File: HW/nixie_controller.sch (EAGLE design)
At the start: 200 parts, among them IC1 INA138, IC10 LD1117S33TR, IC11 74HC595D, IC2 LM386M-1, IC3 7812TV, IC4 DG408DYTSSOP-16, IC5 OPA317DBV, IC6 OPA317DBV, IC7 OPA340U, IC8 OPA340U, IC9 NE555D, J1 POWER_JACKPTH_LOCK, Q10 DMP3099L-7, Q11 MMBT3906, Q2 CMPT5551, Q3 CMPT5551, Q4 CMPT5551, Q5 FMMT558QTA, Q6 CMPT5551, Q7 MMBT3906, Q8 CMPT5551, Q9 CMPT5551, T1 MMBT3904, T2 MMBT3904

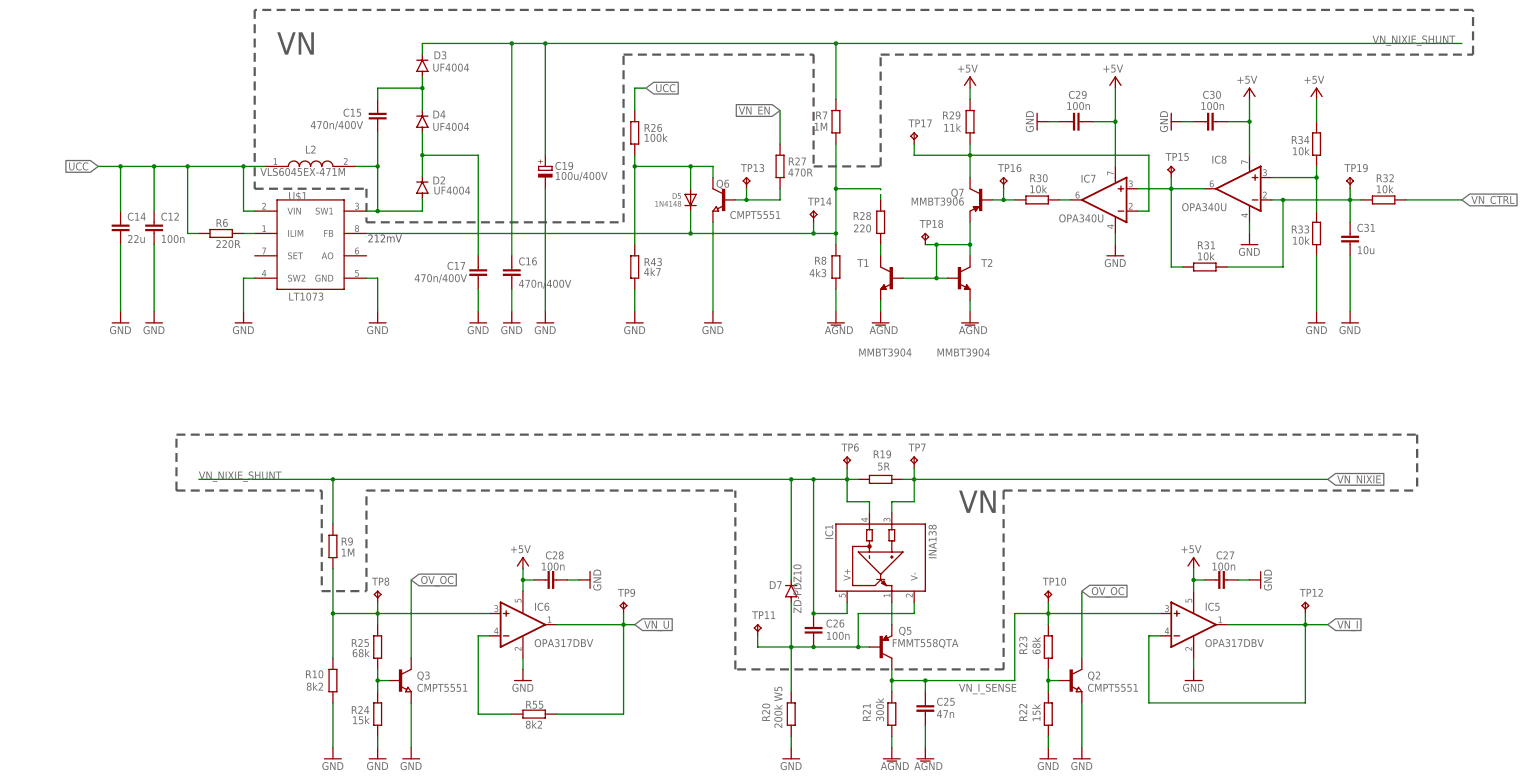
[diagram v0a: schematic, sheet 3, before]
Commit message: Update HW, SW - hlavne SW blizke HW, hodiny funkcni, bezi testovaci sekvence, na zmacknuti tlacitka se zobrazi
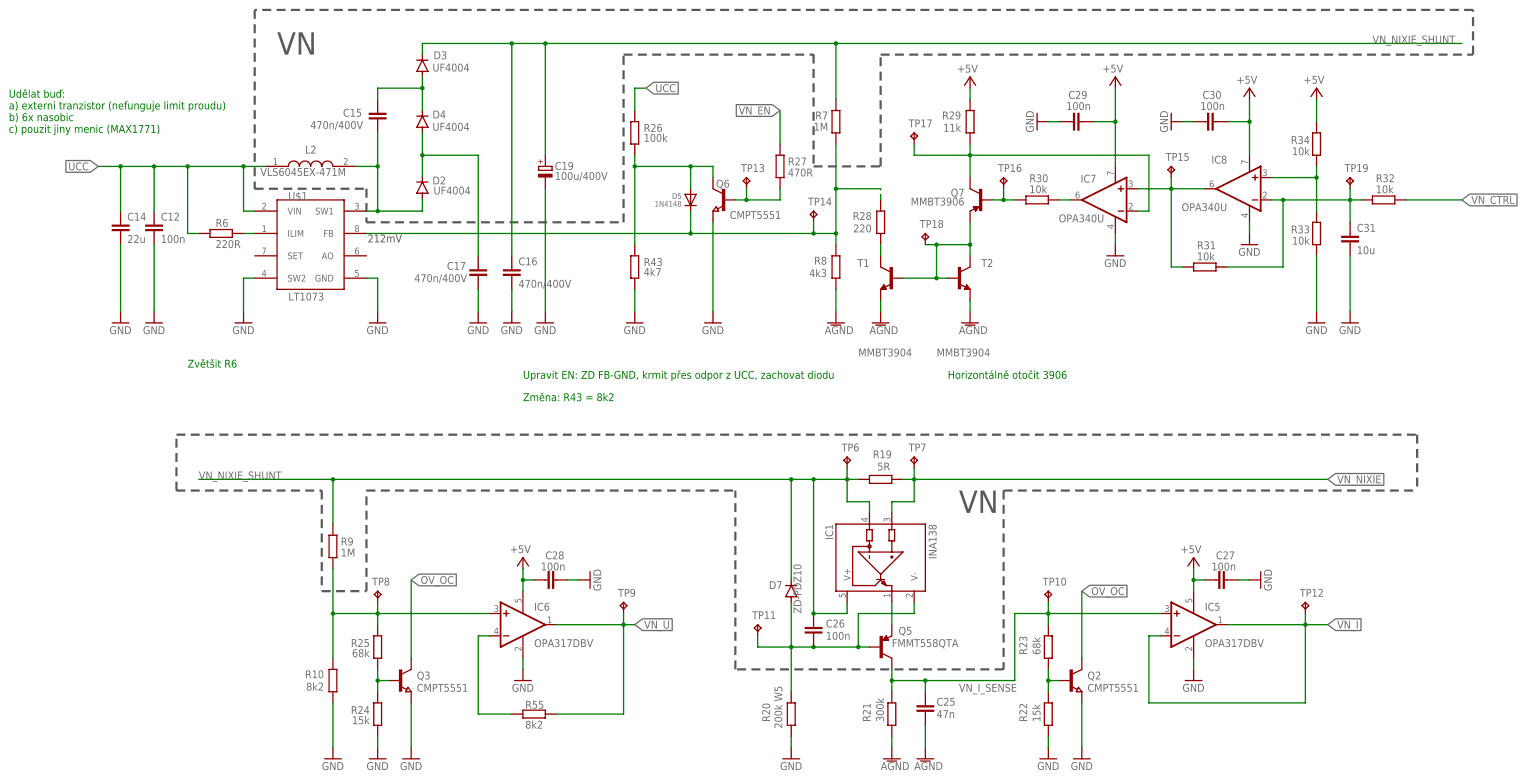
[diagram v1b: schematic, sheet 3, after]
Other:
- note added: "Horizontálně otočit 3906"
- note added: "TAB musi být spojen na VOUT"
- note added: "Udělat buď: a) externi tranzistor (nefunguje limit proudu) b) 6x nasobic c) pouzit jiny menic (MAX1771)"
- note added: "Upravit EN: ZD FB-GND, krmit přes odpor z UCC, zachovat diodu"
- note added: "Změna: R43 = 8k2"
- note added: "Změna: R60 = 1k5"
- note added: "Zvětšit R6"
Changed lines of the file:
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@@
 <text x="129.54" y="208.28" size="1.778" layer="97" ratio="7">GW22LCV
 </text>
+<text x="299.72" y="215.9" size="1.778" layer="91">TAB musi být spojen na VOUT</text>
 </plain>
 <instances>
@@
 <wire x1="337.82" y1="142.24" x2="337.82" y2="129.54" width="0.508" layer="97" style="longdash"/>
 <text x="78.74" y="228.6" size="5.08" layer="97">VN</text>
+<text x="134.62" y="154.94" size="1.778" layer="91">Upravit EN: ZD FB-GND, krmit přes odpor z UCC, zachovat diodu</text>
+<text x="134.62" y="149.86" size="1.778" layer="91">Změna: R43 = 8k2</text>
+<text x="231.14" y="154.94" size="1.778" layer="91">Horizontálně otočit 3906</text>
+<text x="17.78" y="210.82" size="1.778" layer="91">Udělat buď:
+a) externi tranzistor (nefunguje limit proudu)
+b) 6x nasobic
+c) pouzit jiny menic (MAX1771)</text>
+<text x="58.42" y="157.48" size="1.778" layer="91">Zvětšit R6</text>
 </plain>
 <instances>
@@
 <plain>
 <wire x1="83.82" y1="111.76" x2="109.22" y2="111.76" width="0.1524" layer="97" style="shortdash"/>
+<text x="246.38" y="167.64" size="1.778" layer="91">Změna: R60 = 1k5</text>
 </plain>
 <instances>

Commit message: schemata, deska
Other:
- note removed: "71-CRCW1206-2.7K-E3 80-C1206C104M5R"
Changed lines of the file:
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@@
 <description>Controll</description>
 <plain>
-<text x="7.62" y="233.68" size="1.778" layer="91">
-71-CRCW1206-2.7K-E3
-80-C1206C104M5R
-</text>
 </plain>
 <instances>
